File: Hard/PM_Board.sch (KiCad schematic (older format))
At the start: 52 parts

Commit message: [add] フットプリントの割当を完了
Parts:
- removed C?: 9p, symbol Device:C_Small
- removed R? (x2): 22, symbol Device:R_Small
- removed R? (x3): 10k, symbol Device:R_Small
- removed R? (x2): 47k, symbol Device:R_Small
- removed R? (x2): 4.7, symbol Device:R_Small
- removed R?: 1k, symbol Device:R_Small
- added C12: 9p, Capacitor_SMD:C_0402_1005Metric, symbol Device:C_Small
- added C24: 470u, Capacitor_SMD:CP_Elec_10x10, symbol Device:CP_Small
- added C25: 100u, Capacitor_SMD:CP_Elec_6.3x7.7, symbol Device:CP_Small
- added C26: 1u, Capacitor_SMD:C_0402_1005Metric, symbol Device:C_Small
- added D1: Yellow, LED_SMD:LED_0603_1608Metric, symbol Device:LED_Small
- added D2: Blue, LED_SMD:LED_0603_1608Metric, symbol Device:LED_Small
- added D3: Orange, LED_SMD:LED_0603_1608Metric, symbol Device:LED_Small
- added R1, R13, R2, R3: 1k, Resistor_SMD:R_0402_1005Metric, symbol Device:R_Small
- added R12: 56, Resistor_SMD:R_0402_1005Metric, symbol Device:R_Small
- added R14, R15, R16: 10k, Resistor_SMD:R_0402_1005Metric, symbol Device:R_Small
- added R5: 22, Resistor_SMD:R_0402_1005Metric, symbol Device:R_Small
- added R6, R7: 47k, Resistor_SMD:R_0402_1005Metric, symbol Device:R_Small
- added R8, R9: 4.7, Resistor_SMD:R_0402_1005Metric, symbol Device:R_Small
- C1, C10, C13, C14, C15, C16, C17, C18, C19, C2, C20, C21, C22, C3, C4, C5, C6, C7, C8, C9: renamed from C?; Link (none) -> https://www.digikey.jp/product-detail/ja/murata-electronics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
- C11: renamed from C?; footprint (none) -> Capacitor_SMD:C_0402_1005Metric; Agency (none) -> Digkey; Link (none) -> https://www.digikey.jp/product-detail/ja/murata-electronics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; MPN (none) -> GRM1555C1H9R0DA01D; Value (none) -> 9pF
- C23: renamed from C?; footprint (none) -> Capacitor_SMD:C_0402_1005Metric; Agency (none) -> Digikey; Link (none) -> https://www.digikey.jp/product-detail/ja/murata-electronics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; MPN (none) -> GRM155R71H472KA01D; Value (none) -> 4700pF
- D4: renamed from D?; footprint (none) -> KUTKiCad_footprint:DFN5_5x6_1.27P; symbol Device:D_Schottky -> Device:D_Schottky_Small; Agency (none) -> Digikey; Link (none) -> https://www.digikey.jp/product-detail/ja/on-semiconductor/N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; agency Digikey -> (none)
- J1: renamed from J?; Link (none) -> http://akizukidenshi.com/catalog/g/gC-02395/
- J101, J102: renamed from J?; footprint (none) -> MountingHole:MountingHole_2.2mm_M2_Pad_Via
- J2: renamed from J?; footprint (none) -> KUTKiCad_footprint:JST_JQ_05JQ-BT_1x05_P2.5mm_Vertical; Link (none) -> https://www.digikey.jp/products/ja?keywords=05JQ-BT
- J3: renamed from J?; footprint (none) -> KUTKiCad_footprint:Hirose_ZX_ZX62D-B-5P8; Link (none) -> https://www.digikey.jp/product-detail/ja/hirose-electric-co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
- J4, J5: renamed from J?; Agency chip1stop -> Digikey; Link (none) -> https://www.digikey.jp/product-detail/ja/jst-sales-america-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
- J6: renamed from J?; footprint (none) -> KUTKiCad_footprint:Hirose_DF33-DF33C-4DP-3.3DSA_2x02_P3.3mm_Vertical; Link (none) -> https://www.digikey.jp/products/ja?keywords=DF33C-4DP-3.3DS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
- Q1: renamed from Q?; value NMOSFET -> RSS100N03; footprint (none) -> Package_SO:SOIC-8_3.9x4.9mm_P1.27mm; Agency (none) -> 秋月電子; Link (none) -> http://akizukidenshi.com/catalog/g/gI-06376/; MPN (none) -> RSS100N03FRA
- R10: renamed from R?; Link (none) -> https://www.digikey.jp/product-detail/ja/rohm-semiconductor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
- R11: renamed from R?; value 22 -> 56; footprint (none) -> Resistor_SMD:R_0402_1005Metric; Agency (none) -> Digkey; Link (none) -> https://www.digikey.jp/product-detail/ja/panasonic-electron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; MPN (none) -> ERJ-2GEJ560X; Value (none) -> 56Ω
- R4: renamed from R?; footprint (none) -> Resistor_SMD:R_0402_1005Metric; Agency (none) -> Digikey; Link (none) -> https://www.digikey.jp/product-detail/ja/panasonic-electron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; MPN (none) -> ERJ-2GEJ220X; Value (none) -> 22Ω
- U1: renamed from U?; footprint (none) -> KUTKiCad_footprint:Cypress_QFN-68_EP_8x8_Pitch0.4mm; Link (none) -> https://www.digikey.jp/product-detail/ja/cypress-semiconduc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
- U2: renamed from U?; Link (none) -> https://www.digikey.jp/product-detail/ja/texas-instruments/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
- U3: renamed from U?; footprint (none) -> Package_DFN_QFN:DFN-8-1EP_3x3mm_P0.65mm_EP1.55x2.4mm; Agency (none) -> Digikey; Link (none) -> https://www.digikey.jp/product-detail/ja/on-semiconductor/N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; MPN (none) -> NCV7342MW3R2G
- VR1, VR2: renamed from U?; Link (none) -> https://www.digikey.jp/product-detail/ja/on-semiconductor/N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
- Y1: renamed from Y?; footprint (none) -> KUTKiCad_footprint:Crystal_Murata_XRCHA; Link (none) -> https://www.digikey.jp/product-detail/ja/murata-electronics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
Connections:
- wire segments 235 -> 255
- no-connect marks 8 -> 9
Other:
- moved on the sheet: C15, C16, C17, C18, C19, C20, J101, J102, J6, R10, U2, VR1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

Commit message: [add] PCBの基板外形を作った
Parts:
- J1: footprint (none) -> Connector_Card:microSD_HC_Hirose_DM3AT-SF-PEJM5
- J5: footprint Connector_JST:JST_XH_S4B-XH-A_1x04_P2.50mm_Horizontal -> Connector_JST:JST_XH_S4B-XH-A-1_1x04_P2.50mm_Horizontal
- J6: footprint KUTKiCad_footprint:Hirose_DF33-DF33C-4DP-3.3DSA_2x02_P3.3mm_Vertical -> KUTKiCad_footprint:Hirose_DF33-DF33C-4DP-3.3DSA_2x02_P3.3_Vertical
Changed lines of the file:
@@
 	3700 4350 3700 4500
 Connection ~ 3700 4500
-$Comp
-L Connector:Micro_SD_Card_Det_Hirose_DM3AT J1
-U 1 1 5D9DC367
-P 10250 1700
-F 0 "J1" H 10200 2517 50  0000 C CNN
-F 1 "Micro_SD_Card_Det_Hirose_DM3AT" H 10200 2426 50  0000 C CNN
-F 2 "" H 12300 2400 50  0001 C CNN
-F 3 "https://www.hirose.com/product/en/download_file/key_name/DM3/category/Catalog/doc_file_id/49662/?file_category_id=4&item_id=195&is_series=1" H 10250 1800 50  0001 C CNN
-F 4 "秋月電子" H 10250 1700 50  0001 C CNN "Agency"
-F 5 "DM3AT-SF-PEJM5" H 10250 1700 50  0001 C CNN "MPN"
-F 6 "http://akizukidenshi.com/catalog/g/gC-02395/" H 10250 1700 50  0001 C CNN "Link"
-	1    10250 1700
-	1    0    0    -1
-$EndComp
 Wire Wire Line
 	9350 2000 9000 2000
@@
 F 0 "J6" H 1550 1100 50  0000 C CNN
 F 1 "KRC_Conn_CAN" H 1200 800 50  0000 C CNN
-F 2 "KUTKiCad_footprint:Hirose_DF33-DF33C-4DP-3.3DSA_2x02_P3.3mm_Vertical" H 1050 1100 50  0001 C CNN
+F 2 "KUTKiCad_footprint:Hirose_DF33-DF33C-4DP-3.3DSA_2x02_P3.3_Vertical" H 1050 1100 50  0001 C CNN
 F 3 "https://www.hirose.com/product/document?clcode=&productname=&series=DF33C&documenttype=Catalog&lang=ja&documentid=D51103_ja" H 1050 1100 50  0001 C CNN
 F 4 "Digikey" H 1050 1100 50  0001 C CNN "Agency"
@@
 F 0 "J5" H 1800 6350 50  0000 C CNN
 F 1 "KRC_Conn_CAN" H 1450 6050 50  0000 C CNN
-F 2 "Connector_JST:JST_XH_S4B-XH-A_1x04_P2.50mm_Horizontal" H 1300 6350 50  0001 C CNN
+F 2 "Connector_JST:JST_XH_S4B-XH-A-1_1x04_P2.50mm_Horizontal" H 1300 6350 50  0001 C CNN
 F 3 "http://download.siliconexpert.com/pdfs/2014/12/9/8/14/1/458/jst_/manual/29exh.pdf" H 1300 6350 50  0001 C CNN
 F 4 "Digikey" H 1300 6350 50  0001 C CNN "Agency"
@@
 	1    0    0    -1
 $EndComp
+$Comp
+L Connector:Micro_SD_Card_Det_Hirose_DM3AT J1
+U 1 1 5D9DC367
+P 10250 1700
+F 0 "J1" H 10200 2517 50  0000 C CNN
+F 1 "Micro_SD_Card_Det_Hirose_DM3AT" H 10200 2426 50  0000 C CNN
+F 2 "Connector_Card:microSD_HC_Hirose_DM3AT-SF-PEJM5" H 12300 2400 50  0001 C CNN
+F 3 "https://www.hirose.com/product/en/download_file/key_name/DM3/category/Catalog/doc_file_id/49662/?file_category_id=4&item_id=195&is_series=1" H 10250 1800 50  0001 C CNN
+F 4 "秋月電子" H 10250 1700 50  0001 C CNN "Agency"
+F 5 "DM3AT-SF-PEJM5" H 10250 1700 50  0001 C CNN "MPN"
+F 6 "http://akizukidenshi.com/catalog/g/gC-02395/" H 10250 1700 50  0001 C CNN "Link"
+	1    10250 1700
+	1    0    0    -1
+$EndComp

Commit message: [add] 電源系のダイオードをアンビリカル側にも追加
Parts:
- added D5: NTS1545, KUTKiCad_footprint:DFN5_5x6_1.27P, symbol Device:D_Schottky_Small
- J5: footprint Connector_JST:JST_XH_S4B-XH-A-1_1x04_P2.50mm_Horizontal -> Connector_JST:JST_XH_S4B-XH-A_1x04_P2.50mm_Horizontal
- Q1: symbol Device:Q_NMOS_GDS -> KUTKiCad_symbol:RSS100N03
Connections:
- wire segments 255 -> 256
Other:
- moved on the sheet: C24, C25, C26, D3, D4, J101, J102, R3

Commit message: [add] 部品配置仮完了
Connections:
- net INA226_Aleart is gone; now on net INA226_Alert: R16.2, U1.21 (P12[7]/SIO)
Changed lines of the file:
@@
 INA226_SCL
 Text Label 8650 4400 2    50   ~ 0
-INA226_Aleart
+INA226_Alert
 Wire Wire Line
 	8050 4200 8750 4200

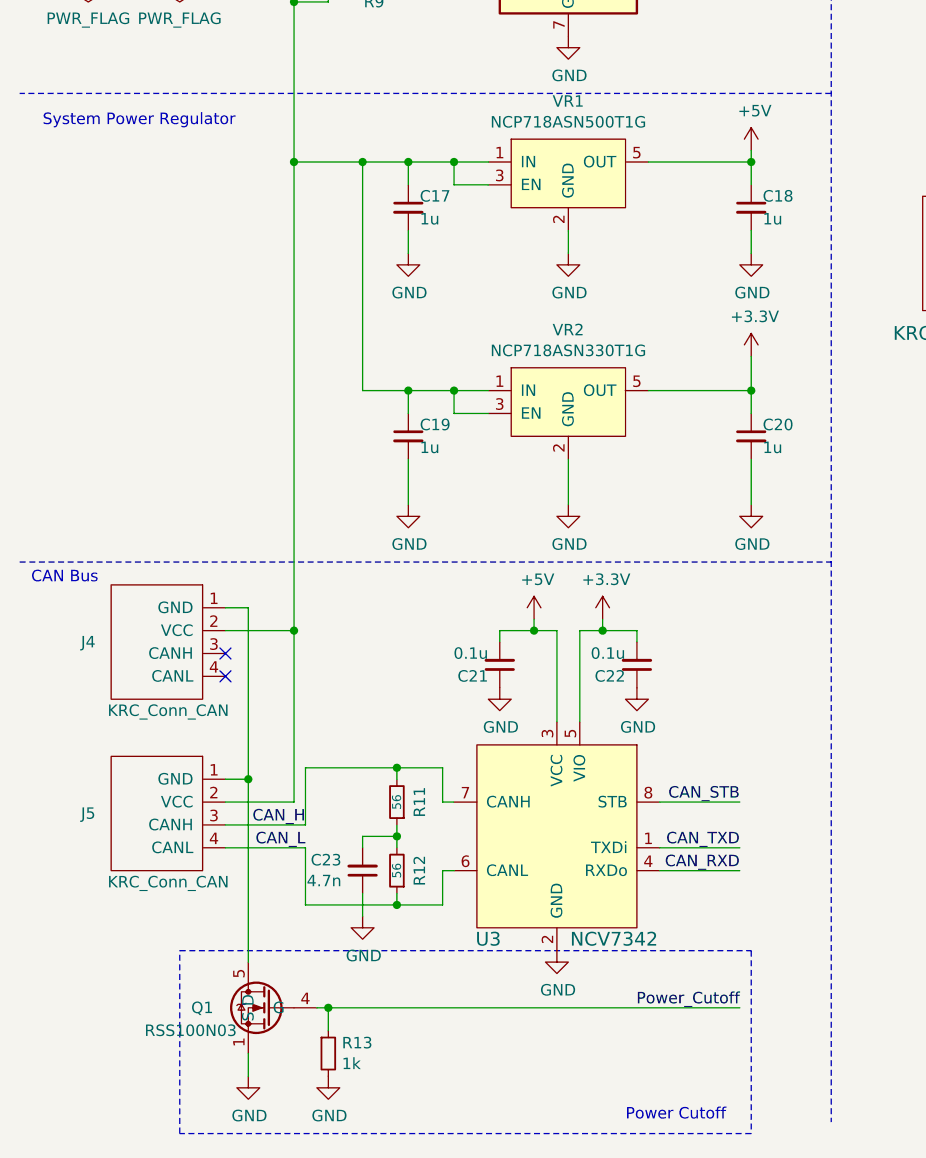
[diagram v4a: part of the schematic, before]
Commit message: [update] カットオフ用のFETをPchに変更してハイサイドへ移動
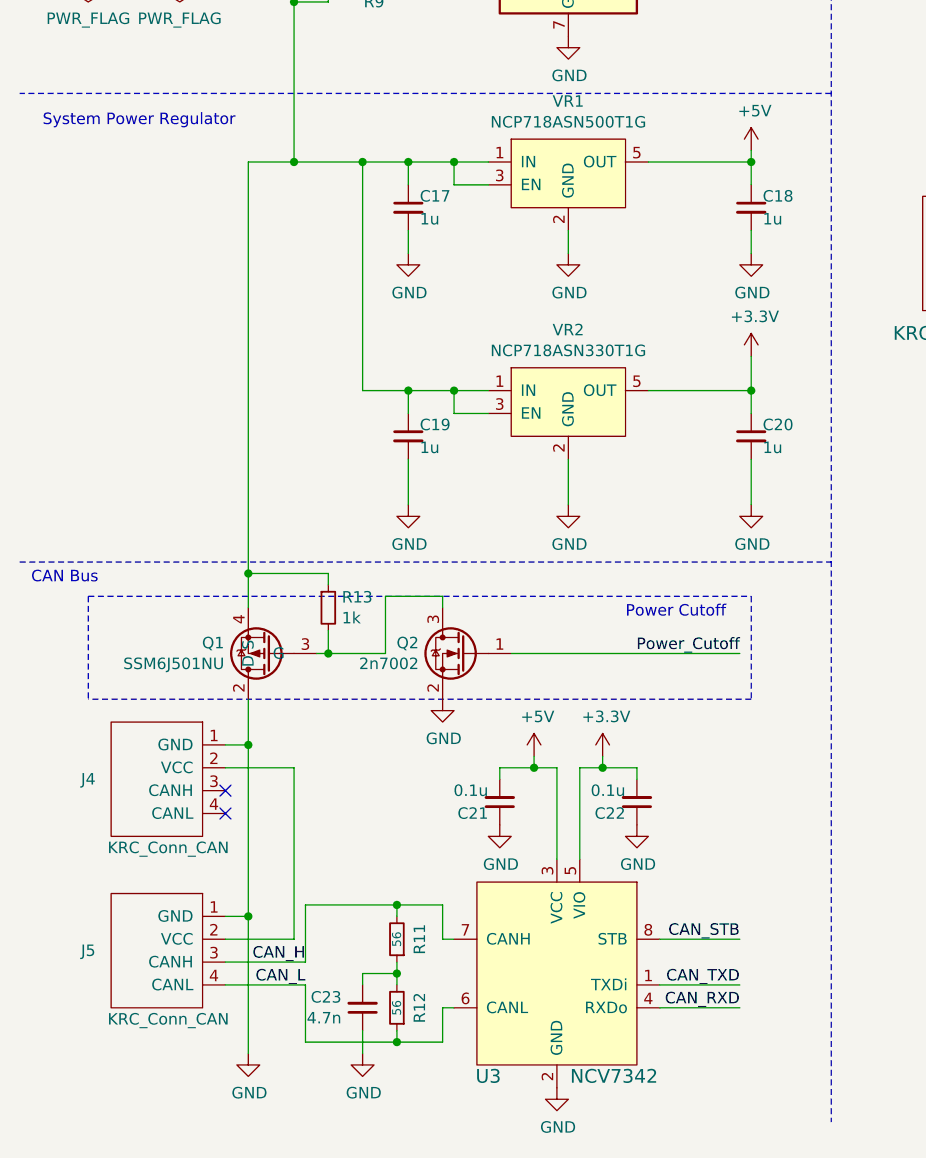
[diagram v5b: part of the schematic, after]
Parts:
- removed Q1: RSS100N03, Package_SO:SOIC-8_3.9x4.9mm_P1.27mm, symbol KUTKiCad_symbol:RSS100N03
- added Q1: SSM6J501NU, KUTKiCad_footprint:UDFN6B, symbol KUTKiCad_symbol:SSM6J501NU
- added Q2: 2n7002, Package_TO_SOT_SMD:SOT-23, symbol Device:Q_NMOS_GSD
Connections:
- net GND: now also J4.1 (GND), J5.1 (GND), Q1.1, Q1.2 (D), Q1.5, Q1.6, Q1.7, Q2.2 (S); no longer R13.2
- net Power_Cutoff: now also Q2.1 (G); no longer R13.1
- net at C17.1, C19.1, R10.2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: now also R13.1, Q1.4 (S), Q1.8; no longer J4.2 (VCC), J5.2 (VCC)
- new net: Q1.3 (G), Q2.3 (D), R13.2
- new net: J4.2 (VCC), J5.2 (VCC)
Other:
- moved on the sheet: C21, C22, C23, J4, J5, R11, R12, R13, U3

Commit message: [update] ミスを修正
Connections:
- net GND: no longer Q1.1, Q1.2 (D), Q1.5, Q1.6, Q1.7
- net at J4.2 (VCC), J5.2 (VCC): now also Q1.1, Q1.2 (D), Q1.5, Q1.6, Q1.7
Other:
- moved on the sheet: Q1, Q2, R13
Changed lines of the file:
@@
 Wire Wire Line
 	1400 6050 1500 6050
-Text Label 3650 5650 2    50   ~ 0
+Text Label 3850 5650 2    50   ~ 0
 Power_Cutoff
 Text Label 3650 6900 2    50   ~ 0
@@
 Text Notes 600  3350 0    50   ~ 0
 System Power Regulator
-Text Notes 550  5350 0    50   ~ 0
+Text Notes 750  5350 0    50   ~ 0
 CAN Bus
-Text Notes 3150 5500 0    50   ~ 0
+Text Notes 3350 5500 0    50   ~ 0
 Power Cutoff
 Text Label 4850 5450 0    50   ~ 0
@@
 L Device:R_Small R13
 U 1 1 5DEF48DF
-P 1850 5450
-F 0 "R13" H 1909 5496 50  0000 L CNN
-F 1 "1k" H 1909 5405 50  0000 L CNN
-F 2 "Resistor_SMD:R_0402_1005Metric" H 1850 5450 50  0001 C CNN
-F 3 "https://b2b-api.panasonic.eu/file_stream/pids/fileversion/1242" H 1850 5450 50  0001 C CNN
-F 4 "Digikey" H 1850 5450 50  0001 C CNN "Agency"
-F 5 "ERJ-2GEJ102X" H 1850 5450 50  0001 C CNN "MPN"
-F 6 "https://www.digikey.jp/product-detail/ja/panasonic-electronic-components/ERJ-2GEJ102X/P1.0KJCT-ND/146897" H 1850 5450 50  0001 C CNN "Link"
-F 7 "1kΩ" H 1850 5450 50  0001 C CNN "Value"
-	1    1850 5450
+P 2050 5450
+F 0 "R13" H 2109 5496 50  0000 L CNN
+F 1 "1k" H 2109 5405 50  0000 L CNN
+F 2 "Resistor_SMD:R_0402_1005Metric" H 2050 5450 50  0001 C CNN
+F 3 "https://b2b-api.panasonic.eu/file_stream/pids/fileversion/1242" H 2050 5450 50  0001 C CNN
+F 4 "Digikey" H 2050 5450 50  0001 C CNN "Agency"
+F 5 "ERJ-2GEJ102X" H 2050 5450 50  0001 C CNN "MPN"
+F 6 "https://www.digikey.jp/product-detail/ja/panasonic-electronic-components/ERJ-2GEJ102X/P1.0KJCT-ND/146897" H 2050 5450 50  0001 C CNN "Link"
+F 7 "1kΩ" H 2050 5450 50  0001 C CNN "Value"
+	1    2050 5450
 	1    0    0    -1
 $EndComp
@@
 L KUTKiCad_symbol:SSM6J501NU Q1
 U 1 1 5D9715A0
-P 1500 5650
-F 0 "Q1" H 1395 5696 50  0000 R CNN
-F 1 "SSM6J501NU" H 1395 5605 50  0000 R CNN
-F 2 "KUTKiCad_footprint:UDFN6B" H 1600 5350 50  0001 C CNN
-F 3 "https://toshiba.semicon-storage.com/jp/product/mosfet/detail.SSM6J501NU.html" H 1600 5350 50  0001 C CNN
-F 4 "Digikey" H 0   0   50  0001 C CNN "Agency"
-F 5 "https://www.digikey.jp/product-detail/ja/toshiba-semiconductor-and-storage/SSM6J501NULF/SSM6J501NULFCT-ND/3191349" H 0   0   50  0001 C CNN "Link"
-F 6 "SSM6J501NU,LF" H 0   0   50  0001 C CNN "MPN"
-	1    1500 5650
+P 1700 5650
+F 0 "Q1" H 1595 5696 50  0000 R CNN
+F 1 "SSM6J501NU" H 1595 5605 50  0000 R CNN
+F 2 "KUTKiCad_footprint:UDFN6B" H 1800 5350 50  0001 C CNN
+F 3 "https://toshiba.semicon-storage.com/jp/product/mosfet/detail.SSM6J501NU.html" H 1800 5350 50  0001 C CNN
+F 4 "Digikey" H 200 0   50  0001 C CNN "Agency"
+F 5 "https://www.digikey.jp/product-detail/ja/toshiba-semiconductor-and-storage/SSM6J501NULF/SSM6J501NULFCT-ND/3191349" H 200 0   50  0001 C CNN "Link"
+F 6 "SSM6J501NU,LF" H 200 0   50  0001 C CNN "MPN"
+	1    1700 5650
 	1    0    0    -1
 $EndComp
@@
 Connection ~ 1500 6800
 $Comp
-L power:GND #PWR?
+L power:GND #PWR0135
 U 1 1 5DA49324
 P 1500 7400
-F 0 "#PWR?" H 1500 7150 50  0001 C CNN
+F 0 "#PWR0135" H 1500 7150 50  0001 C CNN
 F 1 "GND" H 1505 7227 50  0000 C CNN
 F 2 "" H 1500 7400 50  0001 C CNN
@@
 	1    0    0    -1
 $EndComp
-Wire Wire Line
-	1500 5850 1500 6050
-Connection ~ 1500 6050
 Wire Notes Line
-	800  5400 3700 5400
+	1000 5400 3900 5400
 Wire Notes Line
-	3700 5400 3700 5850
+	3900 5400 3900 5850
 Wire Notes Line
-	3700 5850 800  5850
+	3900 5850 1000 5850
 Wire Notes Line
-	800  5400 800  5850
-Wire Wire Line
-	1800 5650 1850 5650
-Wire Wire Line
-	1500 5300 1850 5300
-Wire Wire Line
-	1850 5300 1850 5350
-Connection ~ 1500 5300
-Wire Wire Line
-	1500 5300 1500 5450
-Wire Wire Line
-	1850 5550 1850 5650
-Wire Wire Line
-	1500 3500 1500 5300
-Wire Wire Line
-	1500 3500 1700 3500
-Connection ~ 1700 3500
+	1000 5400 1000 5850
+Wire Wire Line
+	2000 5650 2050 5650
+Wire Wire Line
+	2050 5550 2050 5650
 Wire Wire Line
 	1700 3500 2000 3500
@@
 L Device:Q_NMOS_GSD Q2
 U 1 1 5DB5D4F9
-P 2450 5650
-F 0 "Q2" H 2654 5696 50  0000 L CNN
-F 1 "2n7002" H 2654 5605 50  0000 L CNN
-F 2 "Package_TO_SOT_SMD:SOT-23" H 2650 5750 50  0001 C CNN
-F 3 "http://akizukidenshi.com/download/2n7002.pdf" H 2450 5650 50  0001 C CNN
-F 4 "秋月電子" H 0   0   50  0001 C CNN "Agency"
-F 5 "http://akizukidenshi.com/catalog/g/gI-03919/" H 0   0   50  0001 C CNN "Link"
-F 6 "2N7002" H 0   0   50  0001 C CNN "MPN"
-	1    2450 5650
+P 2650 5650
+F 0 "Q2" H 2854 5696 50  0000 L CNN
+F 1 "2n7002" H 2854 5605 50  0000 L CNN
+F 2 "Package_TO_SOT_SMD:SOT-23" H 2850 5750 50  0001 C CNN
+F 3 "http://akizukidenshi.com/download/2n7002.pdf" H 2650 5650 50  0001 C CNN
+F 4 "秋月電子" H 200 0   50  0001 C CNN "Agency"
+F 5 "http://akizukidenshi.com/catalog/g/gI-03919/" H 200 0   50  0001 C CNN "Link"
+F 6 "2N7002" H 200 0   50  0001 C CNN "MPN"
+	1    2650 5650
 	-1   0    0    -1
 $EndComp
 Wire Wire Line
-	1850 5650 2100 5650
-Wire Wire Line
-	2100 5650 2100 5400
-Wire Wire Line
-	2100 5400 2350 5400
-Connection ~ 1850 5650
-Wire Wire Line
-	2350 5400 2350 5450
-$Comp
-L power:GND #PWR?
+	2050 5650 2300 5650
+Wire Wire Line
+	2300 5650 2300 5400
+Wire Wire Line
+	2300 5400 2550 5400
+Connection ~ 2050 5650
+Wire Wire Line
+	2550 5400 2550 5450
+$Comp
+L power:GND #PWR0136
 U 1 1 5DC40C83
-P 2350 5850
-F 0 "#PWR?" H 2350 5600 50  0001 C CNN
-F 1 "GND" H 2355 5677 50  0000 C CNN
-F 2 "" H 2350 5850 50  0001 C CNN
-F 3 "" H 2350 5850 50  0001 C CNN
-	1    2350 5850
-	1    0    0    -1
-$EndComp
-Wire Wire Line
-	2650 5650 3650 5650
+P 2550 5850
+F 0 "#PWR0136" H 2550 5600 50  0001 C CNN
+F 1 "GND" H 2555 5677 50  0000 C CNN
+F 2 "" H 2550 5850 50  0001 C CNN
+F 3 "" H 2550 5850 50  0001 C CNN
+	1    2550 5850
+	1    0    0    -1
+$EndComp
+Wire Wire Line
+	2850 5650 3850 5650
+Wire Wire Line
+	1700 3500 1700 5150
+Connection ~ 1700 3500
+Wire Wire Line
+	1700 5850 1700 6150
+Connection ~ 1700 6150
+Wire Wire Line
+	2050 5150 1700 5150
+Wire Wire Line
+	2050 5150 2050 5350
+Connection ~ 1700 5150
+Wire Wire Line
+	1700 5150 1700 5450
 $EndSCHEMATC
